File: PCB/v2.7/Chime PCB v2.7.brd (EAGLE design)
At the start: 64.8 x 78.8 mm, 31 parts, among them J1_SPI 1725698, J2_I2C 1725672, J4_A1 282834-3, J5_A0 282834-3, U1 MS5803-02BA, X4 BQ24074

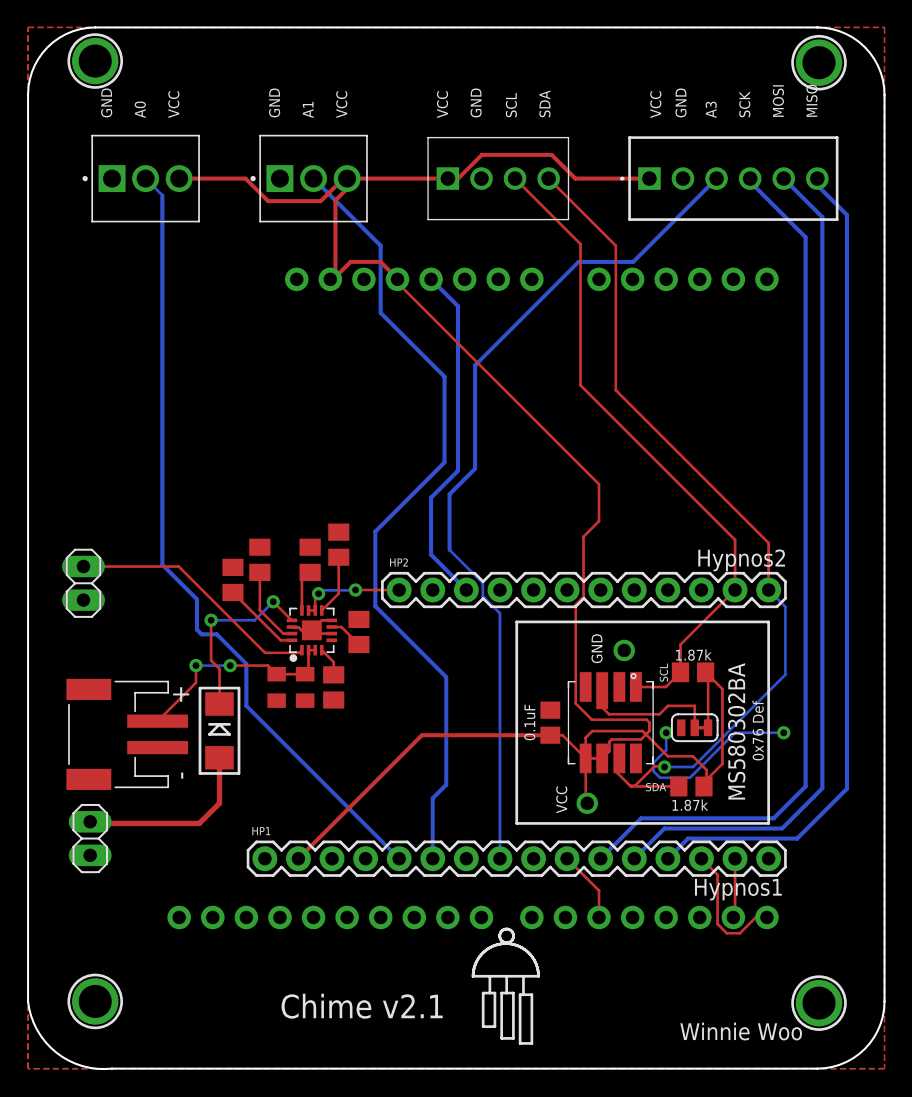
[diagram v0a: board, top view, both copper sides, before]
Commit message: Adding final I2C_Extender and Chime PCB board file
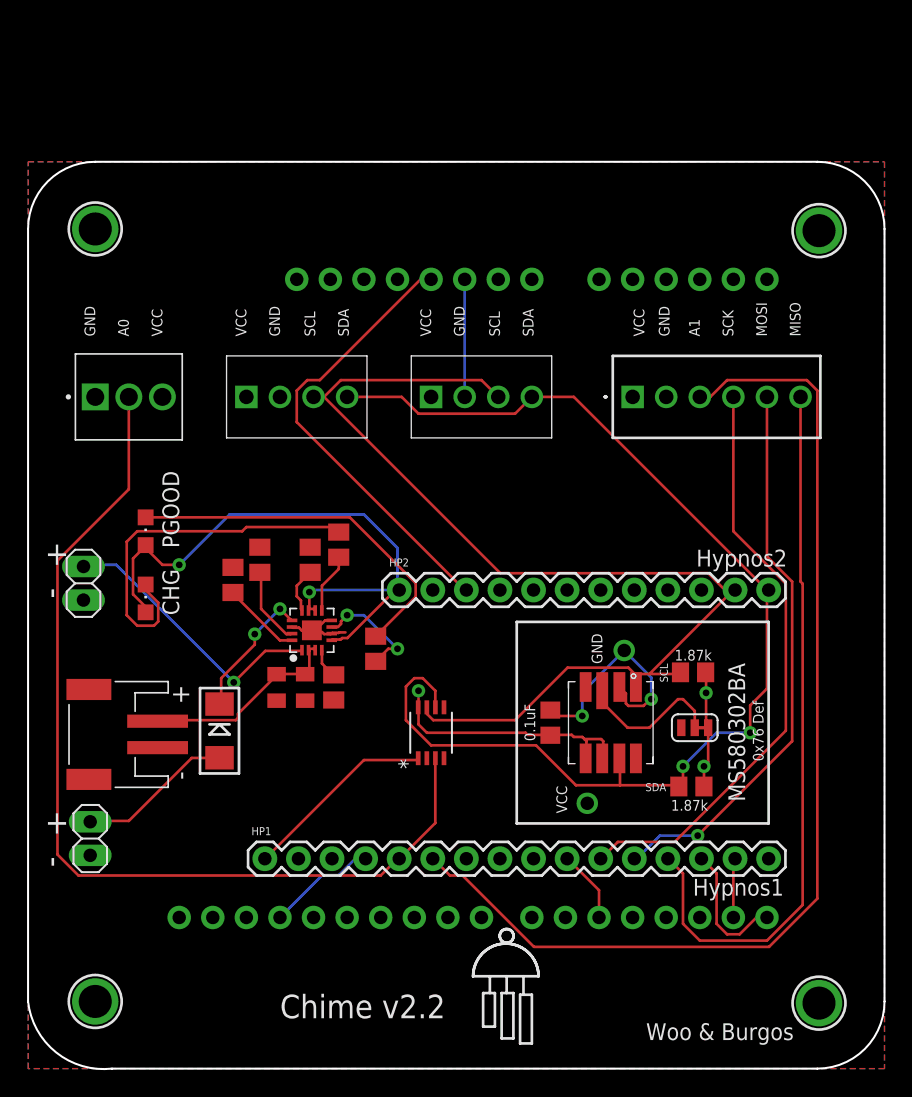
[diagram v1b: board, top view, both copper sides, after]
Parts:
- removed J4_A1: 282834-3, Fixed Terminal Blocks 3P:TE_282834-3
- added CHG: (no value), adafruit:CHIPLED_0805
- added J2_I2C1: 1725672, 1725672:1725672
- added PGOOD: PGOOD, adafruit:CHIPLED_0805
- added U2: S-35770E01I-K8T2U, S-35770 COUNTER:TMSOP08_2P9X2P8_ABL
- R11, R4, R7: value 10K -> 1K
- moved J1_SPI 16.6 mm to (44.5, 49.5)
- moved J2_I2C 16.6 mm to (29.2, 49.5)
- moved J5_A0 16.6 mm to (3.81, 49.5)
- moved U$3 12.7 mm to (3.81, 62.2)
- moved U$4 12.7 mm to (58.5, 62.1)
- moved R11 1.80 mm to (25.0, 30.5)
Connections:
- removed net N$1: X4.5
- new net N$4: PGOOD.C, R11.2
- new net N$5: CHG.C, R7.2
- net A0: now also U2.3
- net A1: now also J1_SPI.3; no longer J4_A1.2
- net A3: no longer J1_SPI.3
- net GND: now also J2_I2C1.2, JP9.2, U2.4; no longer J4_A1.1
- net RST: now also U2.1
- net SCL: now also J2_I2C1.3, U2.7
- net SDA: now also J2_I2C1.4, U2.6
- net VBAT: now also CHG.A, PGOOD.A, X4.5
- net VCC: now also J2_I2C1.1, U2.8; no longer J4_A1.3
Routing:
- net VCC: track 161.6 -> 28.4 mm, vias 0 -> 3
- net A3: track 63.8 -> 0.00 mm
- net VBAT: track 8.09 -> 46.8 mm
- net SCL: track 49.8 -> 85.3 mm
- net N$5: track 0.00 -> 28.3 mm
- net N$4: track 0.00 -> 27.8 mm
- net SDA: track 66.4 -> 89.6 mm, vias 1 -> 2
- net MOSI: track 63.7 -> 42.4 mm, vias 0 -> 1
- net A1: track 60.3 -> 81.5 mm
- net SCK: track 65.5 -> 44.9 mm
- net GND: track 19.8 -> 40.3 mm
- net RST: track 0.00 -> 14.7 mm
- net A0: track 60.1 -> 72.6 mm
- net MISO: track 62.8 -> 54.6 mm
- net 5VRAIL: track 26.3 -> 34.1 mm
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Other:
- board size 64.8 x 78.8 mm -> 64.8 x 68.6 mm
- board text added: "+"
- board text added: "-"
- board text added: "Chime v2.2"
- board text added: "Woo & Burgos"
- board text removed: "A3"
- board text removed: "Chime v2.1"
- board text removed: "Winnie Woo"
